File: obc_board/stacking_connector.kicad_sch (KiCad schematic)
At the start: 37 parts, among them U13 LTC4304CMSTRPBF, U14 PC104, U15 LTC4304CMSTRPBF

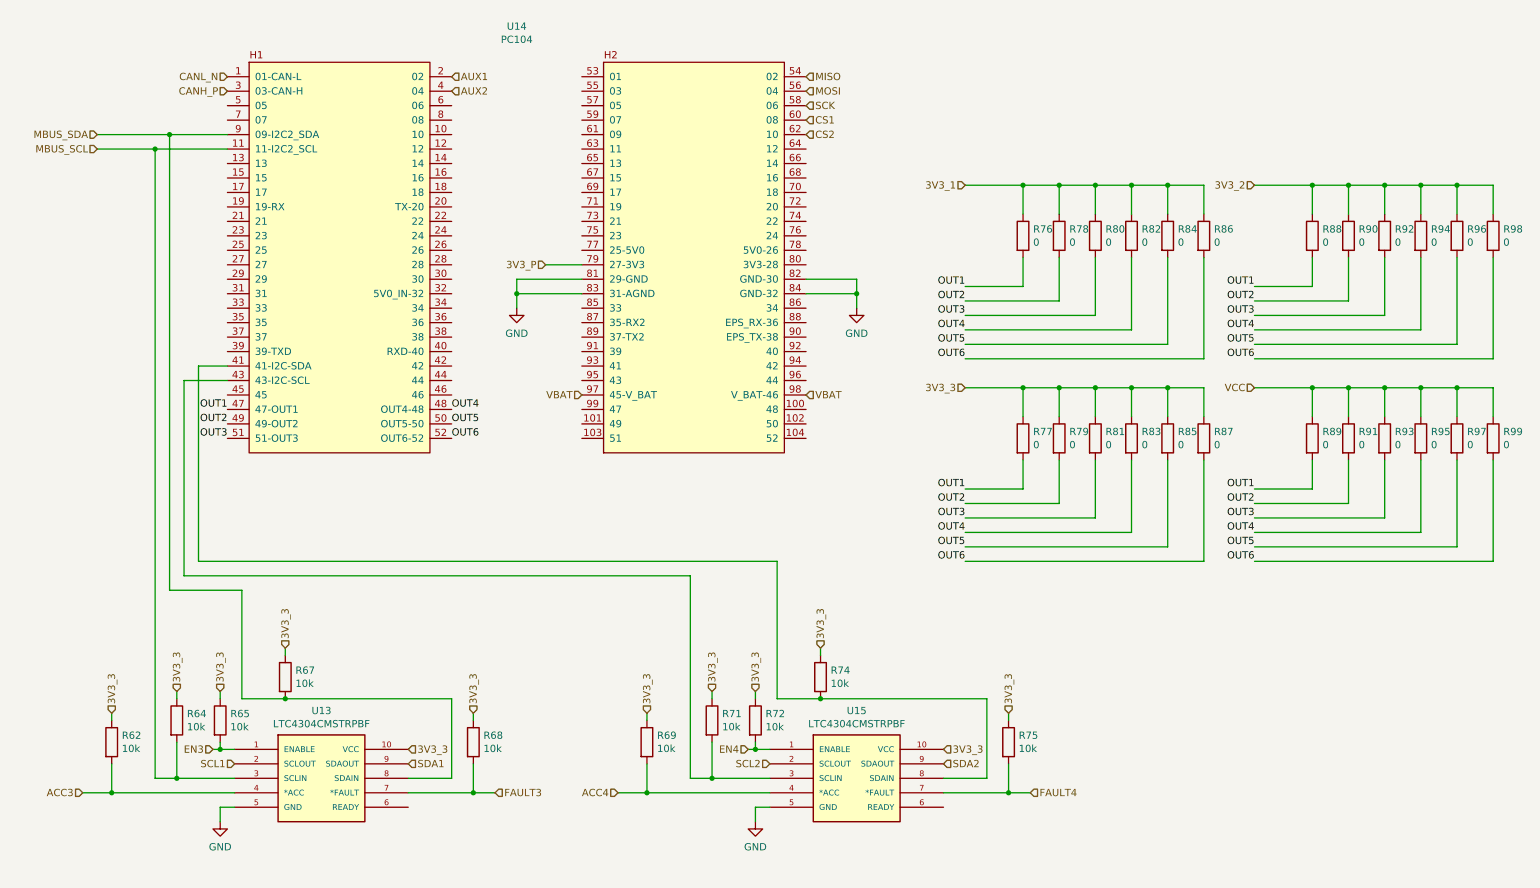
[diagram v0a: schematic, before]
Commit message: changed magnetorquer driver IC and changed power switch IC
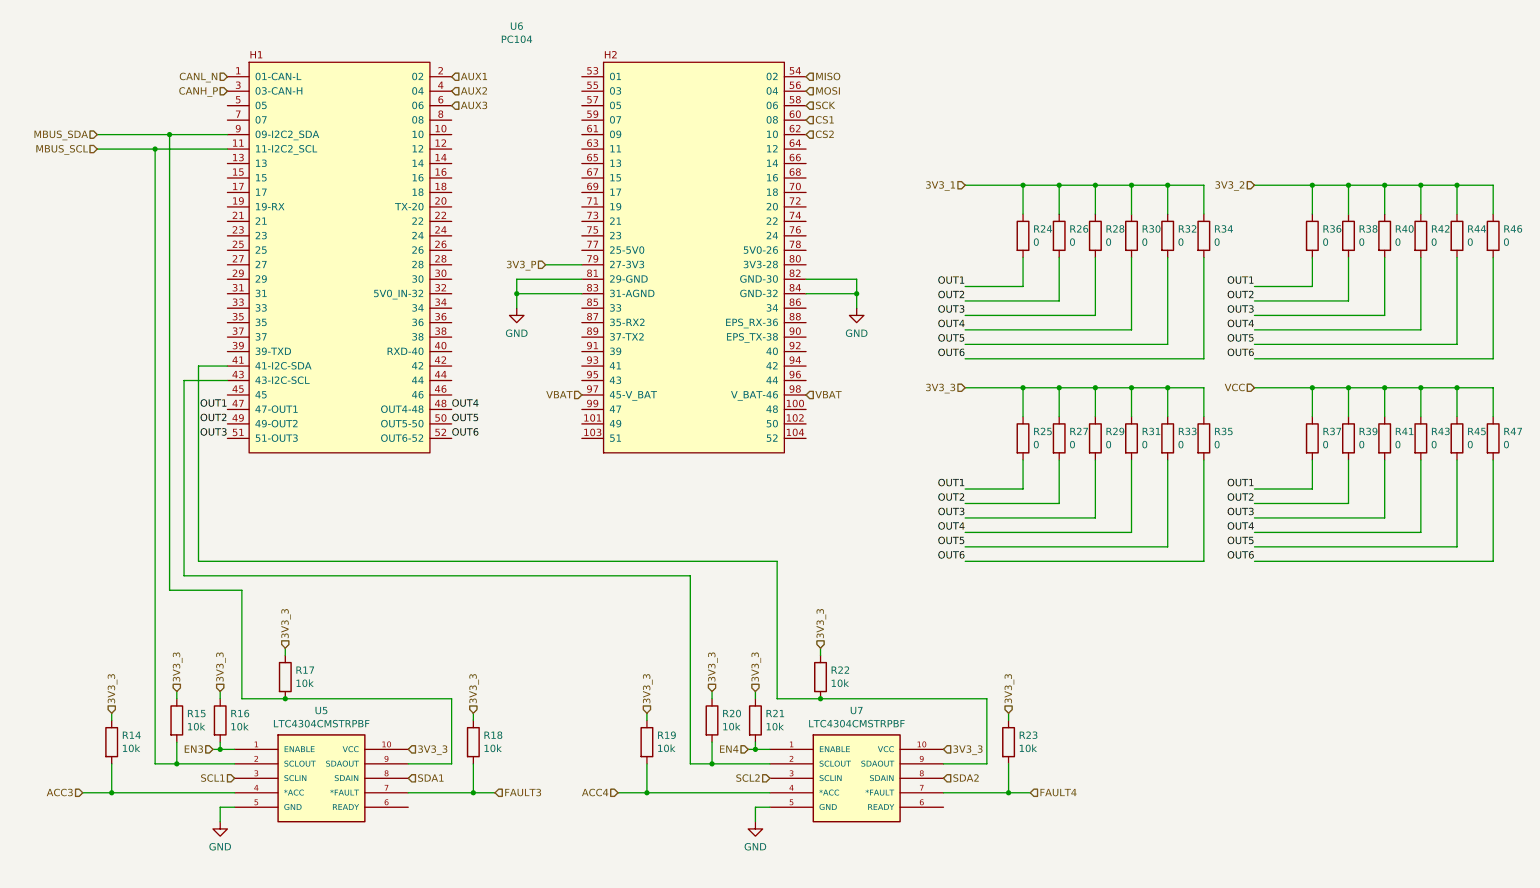
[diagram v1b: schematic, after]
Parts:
- renumbered R62 to R14, R64 to R15, R65 to R16, R67 to R17, R68 to R18, R69 to R19, R71 to R20, R72 to R21, R74 to R22, R75 to R23, R76 to R24, R77 to R25, R78 to R26, R79 to R27, R80 to R28, R81 to R29, R82 to R30, R83 to R31, R84 to R32, R85 to R33, R86 to R34, R87 to R35, R88 to R36, R89 to R37, R90 to R38, R91 to R39, R92 to R40, R93 to R41, R94 to R42, R95 to R43, R96 to R44, R97 to R45, R98 to R46, R99 to R47, U13 to U5, U14 to U6, U15 to U7
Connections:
- net MBUS_SCL: now also U5.2 (SCLOUT); no longer U5.3 (SCLIN)
- net MBUS_SDA: now also U5.9 (SDAOUT); no longer U5.8 (SDAIN)
- net SCL1: now also U5.3 (SCLIN); no longer U5.2 (SCLOUT)
- net SCL2: now also U7.3 (SCLIN); no longer U7.2 (SCLOUT)
- net SDA1: now also U5.8 (SDAIN); no longer U5.9 (SDAOUT)
- net SDA2: now also U7.8 (SDAIN); no longer U7.9 (SDAOUT)
- net at R22.2, U6.41 (41-I2C-SDA): now also U7.9 (SDAOUT); no longer U7.8 (SDAIN)
- net at R20.2, U6.43 (43-I2C-SCL): now also U7.2 (SCLOUT); no longer U7.3 (SCLIN)
- net AUX3: now reaches U6.6 (06)

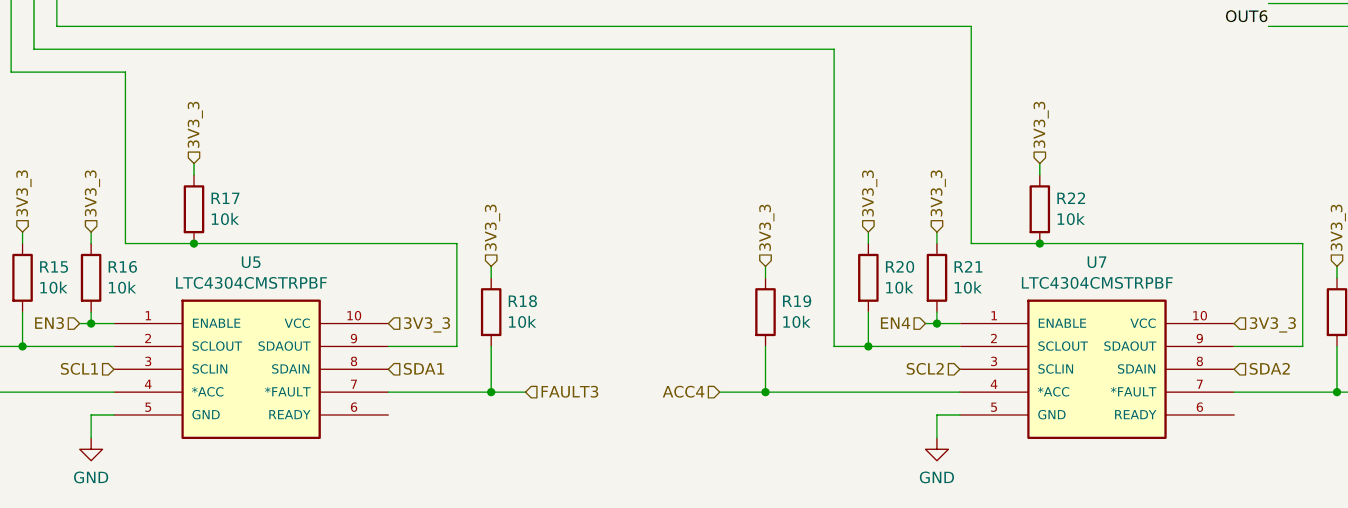
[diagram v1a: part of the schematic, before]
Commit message: updated digikey part numbers and footprints
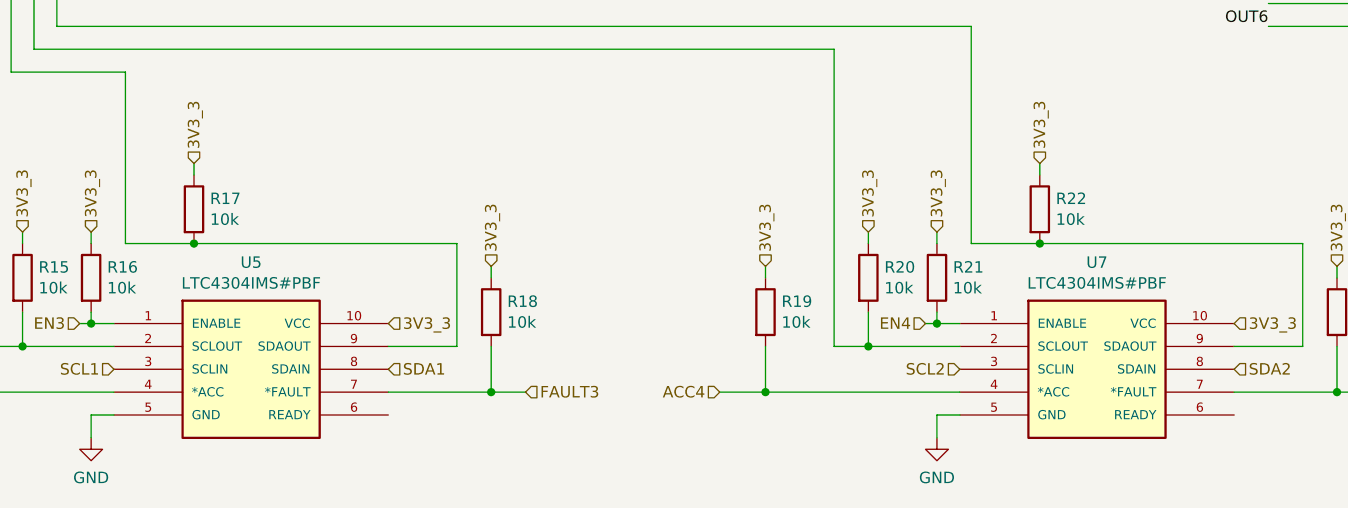
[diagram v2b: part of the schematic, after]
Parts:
- R14, R15, R16, R17, R18, R19, R20, R21, R22, R23: Digikey Part Number 311-10.0KLRCT-ND -> YAG3436CT-ND
- R24, R25, R26, R27, R28, R29, R30, R31, R32, R33, R34, R35, R36, R37, R38, R39, R40, R41, R42, R43, R44, R45, R46, R47: Digikey Part Number 311-0.0JRTR-ND -> 311-0.0LBCT-ND
- U5, U7: value LTC4304CMSTRPBF -> LTC4304IMS#PBF; Digikey Part Number LTC4304CMS#PBF-ND -> LTC4304IMS#PBF-ND

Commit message: updated pcb
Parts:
- U5, U7: footprint MSOP-10_MS -> Package_SO:MSOP-10_3x3mm_P0.5mm
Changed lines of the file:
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@@
     (property "Reference" "U5" (id 0) (at 69.85 141.8082 0))
     (property "Value" "LTC4304IMS#PBF" (id 1) (at 69.85 144.1196 0))
-    (property "Footprint" "MSOP-10_MS" (id 2) (at 54.61 148.59 0)
+    (property "Footprint" "Package_SO:MSOP-10_3x3mm_P0.5mm" (id 2) (at 54.61 148.59 0)
       (effects (font (size 1.27 1.27)) (justify left bottom) hide)
     )
@@
     (property "Reference" "U7" (id 0) (at 163.83 141.8082 0))
     (property "Value" "LTC4304IMS#PBF" (id 1) (at 163.83 144.1196 0))
-    (property "Footprint" "MSOP-10_MS" (id 2) (at 148.59 148.59 0)
+    (property "Footprint" "Package_SO:MSOP-10_3x3mm_P0.5mm" (id 2) (at 148.59 148.59 0)
       (effects (font (size 1.27 1.27)) (justify left bottom) hide)
     )

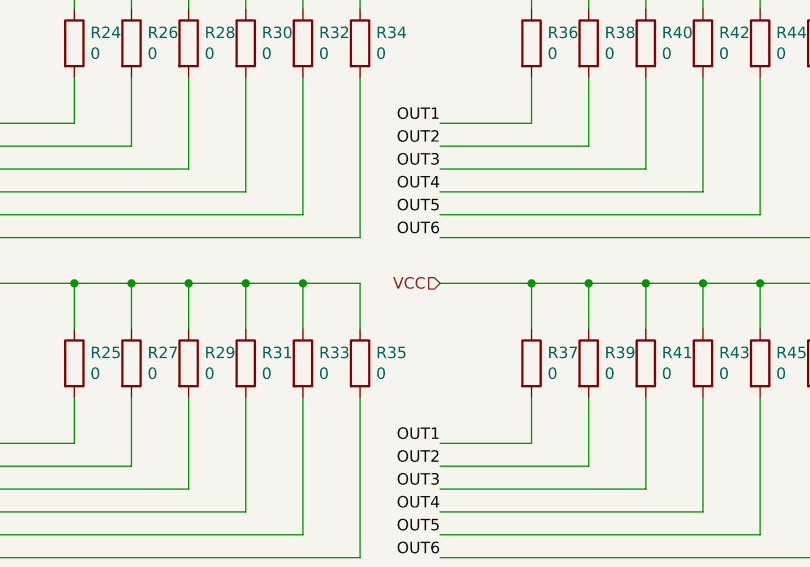
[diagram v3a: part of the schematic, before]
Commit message: routed most of board
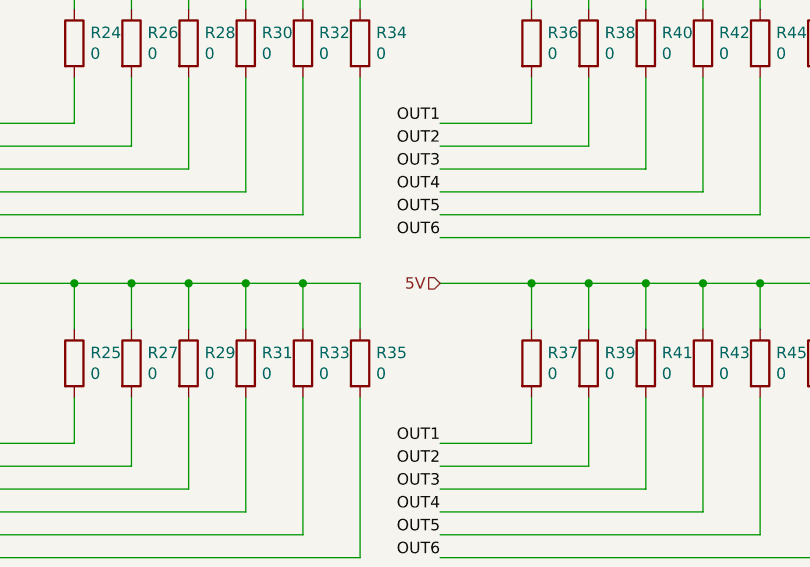
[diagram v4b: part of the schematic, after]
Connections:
- net VCC renamed 5V
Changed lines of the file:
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@@
     (effects (font (size 1.27 1.27)) (justify right))
   )
-  (hierarchical_label "VCC" (shape input) (at 233.68 85.09 180)
+  (hierarchical_label "5V" (shape input) (at 233.68 85.09 180)
     (effects (font (size 1.27 1.27)) (justify right))
   )
@@
       (effects (font (size 1.27 1.27)) (justify left bottom) hide)
     )
-    (property "Datasheet" "https://www.analog.com/media/en/technical-documentation/data-sheets/4304fa.pdf" (id 3) (at 54.61 148.59 0)
+    (property "Datasheet" "ltc4304cms#trpbf" (id 3) (at 54.61 148.59 0)
       (effects (font (size 1.27 1.27)) (justify left bottom) hide)
     )
@@
       (effects (font (size 1.27 1.27)) (justify left bottom) hide)
     )
-    (property "Datasheet" "https://www.analog.com/media/en/technical-documentation/data-sheets/4304fa.pdf" (id 3) (at 148.59 148.59 0)
+    (property "Datasheet" "ltc4304cms#trpbf" (id 3) (at 148.59 148.59 0)
       (effects (font (size 1.27 1.27)) (justify left bottom) hide)
     )

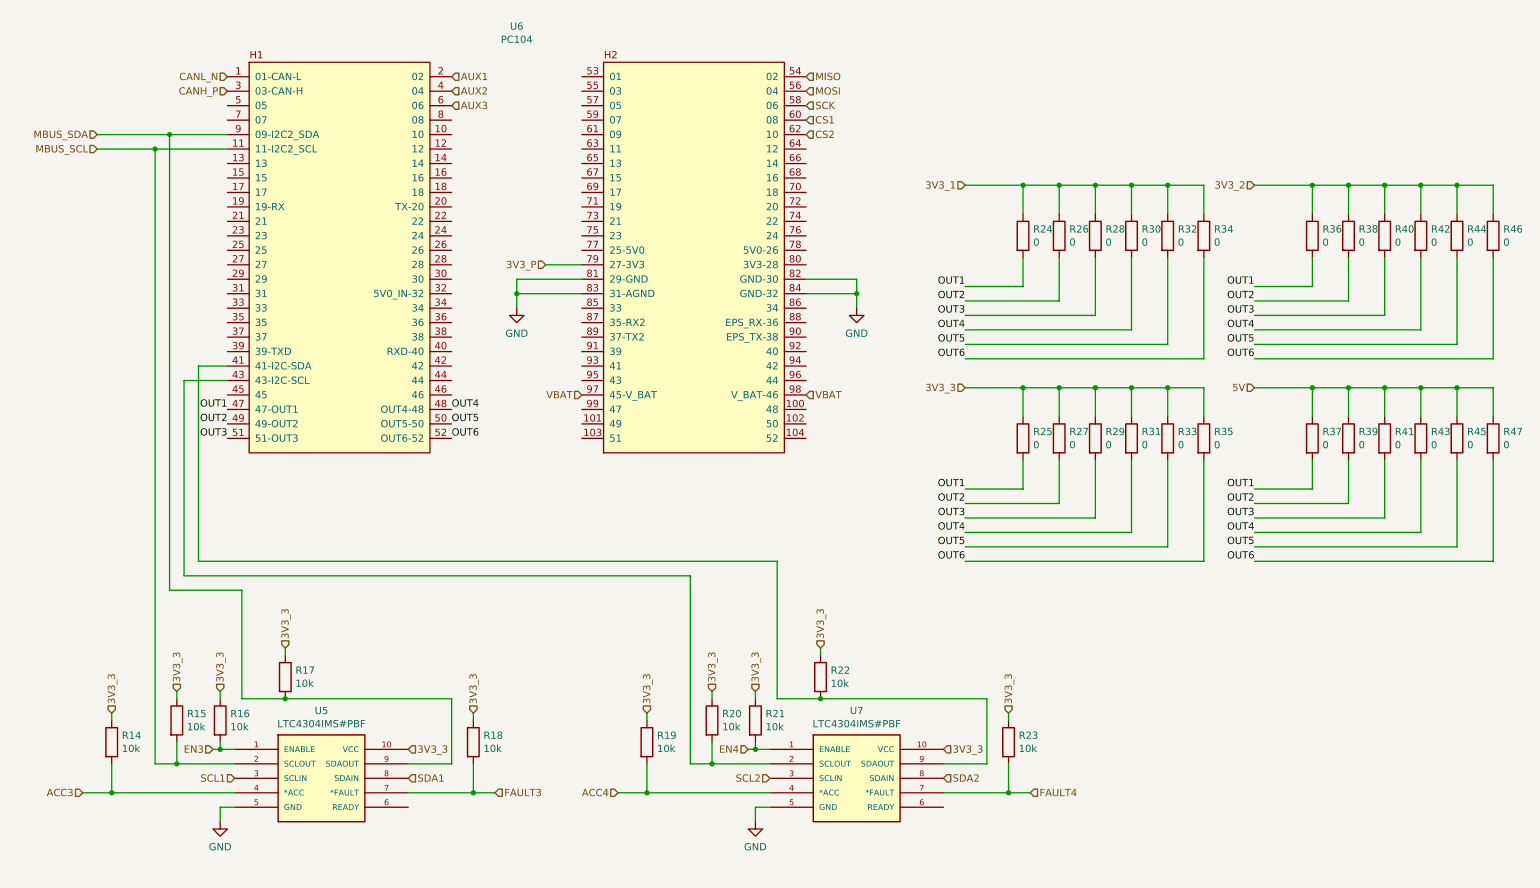
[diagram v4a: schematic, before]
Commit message: added silkscreen labels and gerber file
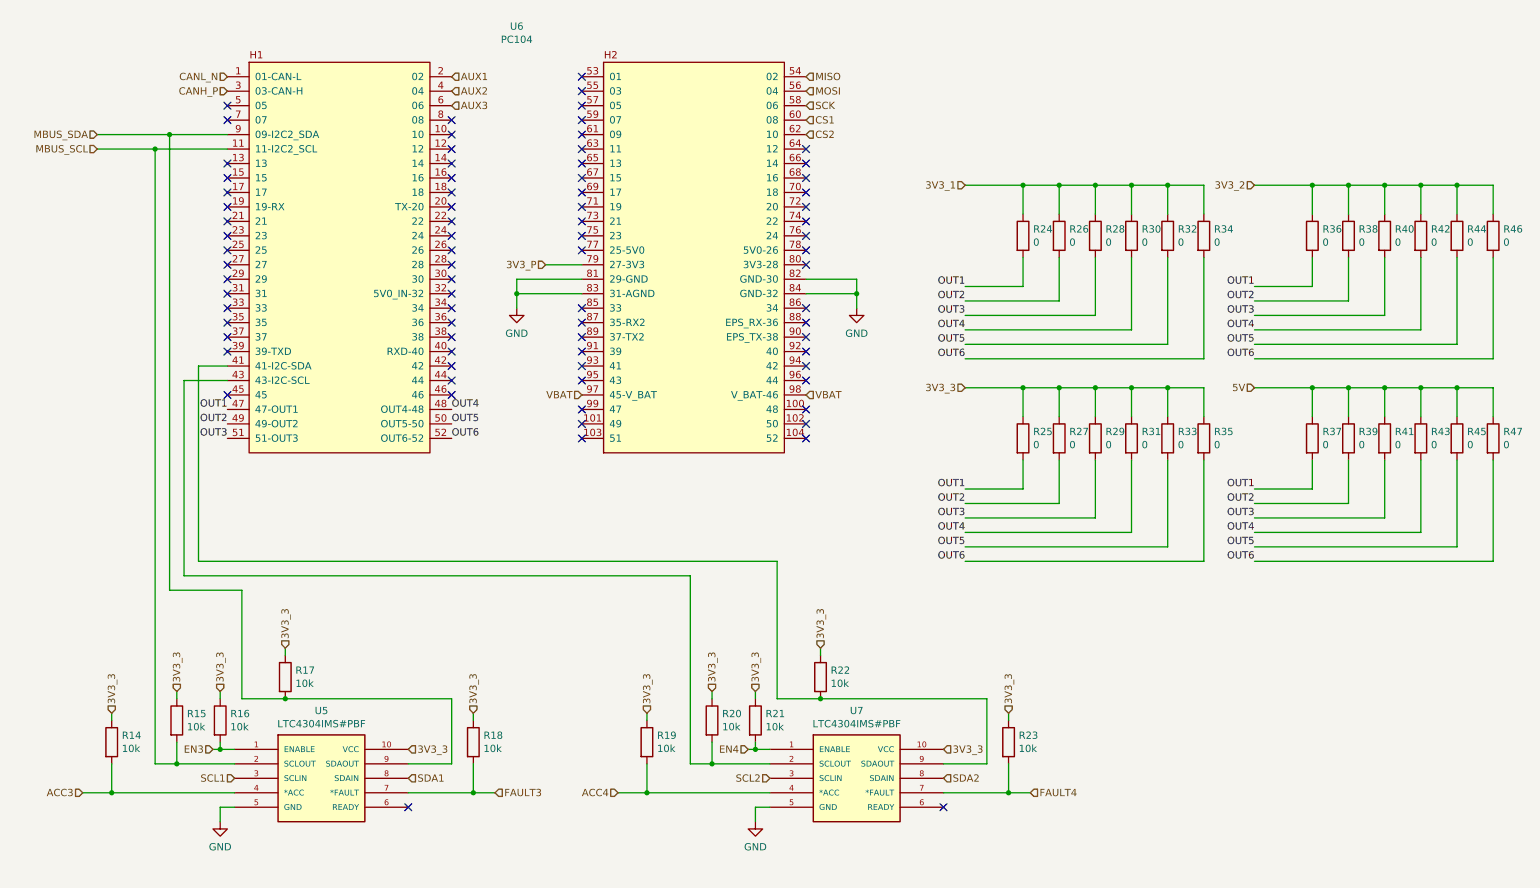
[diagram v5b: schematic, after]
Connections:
- no-connect marks 0 -> 79
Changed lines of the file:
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@@
   (junction (at 269.24 85.09) (diameter 0) (color 0 0 0 0)
   )
+  (no_connect (at 115.57 55.88))
+  (no_connect (at 115.57 58.42))
+  (no_connect (at 115.57 60.96))
+  (no_connect (at 154.94 63.5))
+  (no_connect (at 154.94 71.12))
+  (no_connect (at 154.94 93.98))
+  (no_connect (at 154.94 91.44))
+  (no_connect (at 154.94 88.9))
+  (no_connect (at 154.94 83.82))
+  (no_connect (at 154.94 81.28))
+  (no_connect (at 154.94 78.74))
+  (no_connect (at 154.94 76.2))
+  (no_connect (at 154.94 73.66))
+  (no_connect (at 179.07 158.75))
+  (no_connect (at 85.09 158.75))
+  (no_connect (at 115.57 73.66))
+  (no_connect (at 115.57 76.2))
+  (no_connect (at 115.57 78.74))
+  (no_connect (at 115.57 81.28))
+  (no_connect (at 115.57 83.82))
+  (no_connect (at 115.57 88.9))
+  (no_connect (at 115.57 91.44))
+  (no_connect (at 115.57 93.98))
+  (no_connect (at 115.57 71.12))
+  (no_connect (at 154.94 60.96))
+  (no_connect (at 154.94 58.42))
+  (no_connect (at 154.94 55.88))
+  (no_connect (at 154.94 53.34))
+  (no_connect (at 154.94 50.8))
+  (no_connect (at 154.94 48.26))
+  (no_connect (at 154.94 45.72))
+  (no_connect (at 154.94 43.18))
+  (no_connect (at 53.34 38.1))
+  (no_connect (at 53.34 35.56))
+  (no_connect (at 92.71 40.64))
+  (no_connect (at 92.71 43.18))
+  (no_connect (at 92.71 45.72))
+  (no_connect (at 92.71 48.26))
+  (no_connect (at 92.71 50.8))
+  (no_connect (at 92.71 53.34))
+  (no_connect (at 92.71 55.88))
+  (no_connect (at 92.71 58.42))
+  (no_connect (at 92.71 60.96))
+  (no_connect (at 92.71 63.5))
+  (no_connect (at 92.71 38.1))
+  (no_connect (at 53.34 86.36))
+  (no_connect (at 92.71 66.04))
+  (no_connect (at 92.71 68.58))
+  (no_connect (at 92.71 71.12))
+  (no_connect (at 92.71 73.66))
+  (no_connect (at 92.71 76.2))
+  (no_connect (at 92.71 83.82))
+  (no_connect (at 92.71 86.36))
+  (no_connect (at 53.34 78.74))
+  (no_connect (at 53.34 76.2))
+  (no_connect (at 53.34 73.66))
+  (no_connect (at 53.34 71.12))
+  (no_connect (at 53.34 68.58))
+  (no_connect (at 53.34 66.04))
+  (no_connect (at 53.34 63.5))
+  (no_connect (at 53.34 60.96))
+  (no_connect (at 53.34 58.42))
+  (no_connect (at 53.34 55.88))
+  (no_connect (at 53.34 53.34))
+  (no_connect (at 53.34 50.8))
+  (no_connect (at 53.34 48.26))
+  (no_connect (at 53.34 45.72))
+  (no_connect (at 92.71 78.74))
+  (no_connect (at 92.71 81.28))
+  (no_connect (at 115.57 30.48))
+  (no_connect (at 115.57 33.02))
+  (no_connect (at 115.57 35.56))
+  (no_connect (at 115.57 38.1))
+  (no_connect (at 115.57 40.64))
+  (no_connect (at 115.57 43.18))
+  (no_connect (at 115.57 45.72))
+  (no_connect (at 115.57 48.26))
+  (no_connect (at 115.57 50.8))
+  (no_connect (at 115.57 53.34))
   (wire (pts (xy 138.43 151.13) (xy 148.59 151.13))
     (stroke (width 0) (type default) (color 0 0 0 0))
